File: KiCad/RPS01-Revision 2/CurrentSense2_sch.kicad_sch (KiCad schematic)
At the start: 6 parts

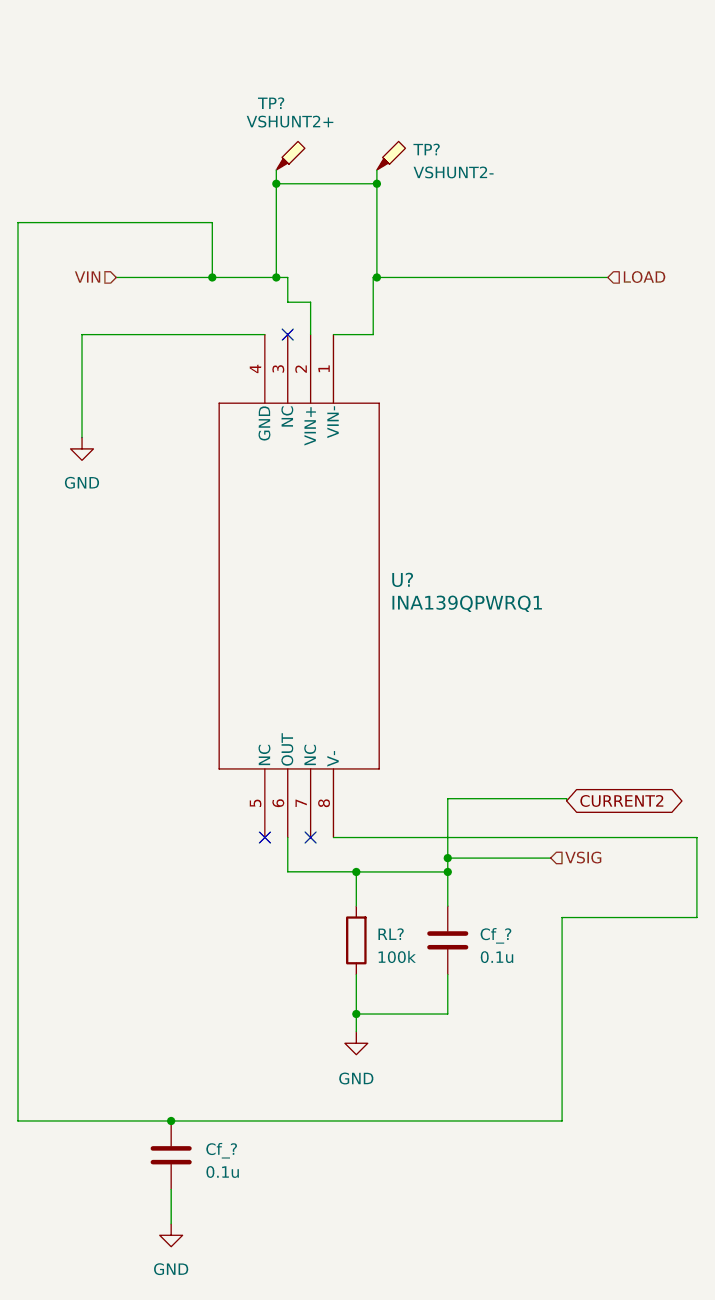
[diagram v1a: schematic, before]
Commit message: Current sense update
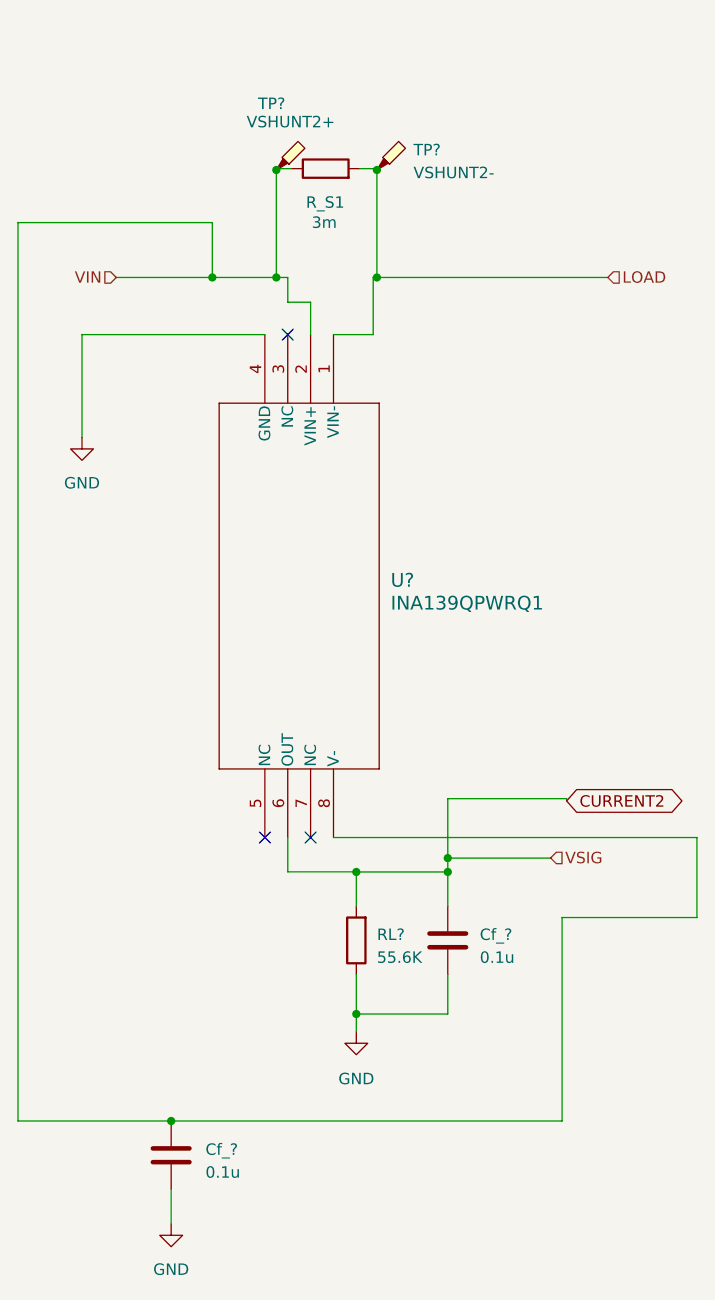
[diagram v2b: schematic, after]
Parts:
- added R_S1: 3m, Mechatronic Footprints:CSS2H-5930R, symbol Device:R
- RL?: value 100k -> 55.6K
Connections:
- net LOAD: now also R_S1.2; no longer Cf_?.1, TP?.1, U?.2 (VIN+), U?.8 (V-)
- new net VIN: Cf_?.1, R_S1.1, TP?.1, U?.2 (VIN+), U?.8 (V-)
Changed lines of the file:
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@@
 (kicad_sch (version 20230121) (generator eeschema)
   (paper "A4")
-  (junction (at 128.524 49.53) (diameter 0) (color 0 0 0 0)
+  (junction (at 128.524 48.006) (diameter 0) (color 0 0 0 0)
   )
   (junction (at 116.84 153.67) (diameter 0) (color 0 0 0 0)
@@
   (junction (at 147.574 124.46) (diameter 0) (color 0 0 0 0)
   )
-  (junction (at 139.7 49.53) (diameter 0) (color 0 0 0 0)
+  (junction (at 139.7 48.006) (diameter 0) (color 0 0 0 0)
   )
   (junction (at 137.414 141.7826) (diameter 0) (color 0 0 0 0)
@@
     (stroke (width 0) (type default))
   )
+  (wire (pts (xy 128.524 47.8536) (xy 128.524 48.006))
+    (stroke (width 0) (type default))
+  )
   (wire (pts (xy 129.794 125.984) (xy 137.414 125.984))
     (stroke (width 0) (type default))
@@
     (stroke (width 0) (type default))
   )
-  (wire (pts (xy 139.7 49.53) (xy 139.7 59.944))
-    (stroke (width 0) (type default))
-  )
-  (wire (pts (xy 128.524 49.53) (xy 139.7 49.53))
+  (wire (pts (xy 139.7 48.006) (xy 139.7 59.944))
     (stroke (width 0) (type default))
   )
@@
     (stroke (width 0) (type default))
   )
-  (wire (pts (xy 128.524 49.53) (xy 128.524 48.006))
+  (wire (pts (xy 130.2004 47.8536) (xy 128.524 47.8536))
     (stroke (width 0) (type default))
   )
@@
     (stroke (width 0) (type default))
   )
+  (wire (pts (xy 137.8204 47.8536) (xy 139.7 47.8536))
+    (stroke (width 0) (type default))
+  )
   (wire (pts (xy 134.874 122.174) (xy 175.26 122.174))
     (stroke (width 0) (type default))
@@
     (stroke (width 0) (type default))
   )
-  (wire (pts (xy 128.524 59.944) (xy 128.524 49.53))
+  (wire (pts (xy 128.524 48.006) (xy 128.524 59.944))
     (stroke (width 0) (type default))
   )
@@
     (stroke (width 0) (type default))
   )
+  (wire (pts (xy 139.7 47.8536) (xy 139.7 48.006))
+    (stroke (width 0) (type default))
+  )
   (wire (pts (xy 147.574 137.414) (xy 147.574 141.7826))
     (stroke (width 0) (type default))
@@
   )
   (wire (pts (xy 147.574 124.46) (xy 147.574 117.856))
-    (stroke (width 0) (type default))
-  )
-  (wire (pts (xy 139.7 48.006) (xy 139.7 49.53))
     (stroke (width 0) (type default))
   )
@@
       (effects (font (size 1.27 1.27)) (justify right))
     )
-    (property "Value" "100k" (at 139.7 135.509 0)
+    (property "Value" "55.6K" (at 139.7 135.509 0)
       (effects (font (size 1.27 1.27)) (justify right))
     )
@@
         )
       )
+    )
+  )
+  (symbol (lib_id "Device:R") (at 134.0104 47.8536 90) (unit 1)
+    (in_bom yes) (on_board yes) (dnp no)
+    (property "Reference" "R_S1" (at 133.9596 51.6128 90)
+      (effects (font (size 1.27 1.27)))
+    )
+    (property "Value" "3m" (at 133.858 53.848 90)
+      (effects (font (size 1.27 1.27)))
+    )
+    (property "Footprint" "Mechatronic Footprints:CSS2H-5930R" (at 134.0104 49.6316 90)
+      (effects (font (size 1.27 1.27)) hide)
+    )
+    (property "Datasheet" "~" (at 134.0104 47.8536 0)
+      (effects (font (size 1.27 1.27)) hide)
+    )
+    (pin "1")
+    (pin "2")
+    (instances
+      (project "rps01"
+        (path "/14930f15-c0a0-4b55-93e6-b112548415f6/13e150ee-6c46-47a5-9c09-3749eb0dcbfe"
+          (reference "R_S1") (unit 1)
+        )
+        (path "/14930f15-c0a0-4b55-93e6-b112548415f6/83d3dc76-6aeb-422d-8708-14a32de244f0"
+          (reference "R_S2") (unit 1)
+        )
+      )

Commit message: Update Current sense references
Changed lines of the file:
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@@
   )
   (symbol (lib_id "Device:R") (at 137.414 133.604 180) (unit 1)
-    (in_bom yes) (on_board yes) (dnp no) (fields_autoplaced)
-    (property "Reference" "RL?" (at 139.7 132.969 0)
+    (in_bom yes) (on_board yes) (dnp no)
+    (property "Reference" "RL?" (at 127 132.08 0)
       (effects (font (size 1.27 1.27)) (justify right))
     )
-    (property "Value" "55.6K" (at 139.7 135.509 0)
+    (property "Value" "55.6K" (at 127 134.62 0)
       (effects (font (size 1.27 1.27)) (justify right))
     )
@@
         )
         (path "/14930f15-c0a0-4b55-93e6-b112548415f6/83d3dc76-6aeb-422d-8708-14a32de244f0"
-          (reference "R31") (unit 1)
+          (reference "R1_CS2") (unit 1)
         )
       )
@@
         )
         (path "/14930f15-c0a0-4b55-93e6-b112548415f6/83d3dc76-6aeb-422d-8708-14a32de244f0"
-          (reference "C22") (unit 1)
+          (reference "C1_CS2") (unit 1)
         )
       )
@@
         )
         (path "/14930f15-c0a0-4b55-93e6-b112548415f6/83d3dc76-6aeb-422d-8708-14a32de244f0"
-          (reference "Cf_1") (unit 1)
-        )
-      )
+          (reference "C2_CS2") (unit 1)
+        )
+      )

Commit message: Only Switches left
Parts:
- removed Cf_?: 0.1u, Capacitor_SMD:C_0603_1608Metric, symbol Device:C
- added R_S1: 3m, Mechatronic Footprints:CSS2H-5930R, symbol Device:R
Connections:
- net LOAD: now also R_S1.2
- net VIN: now also R_S1.1

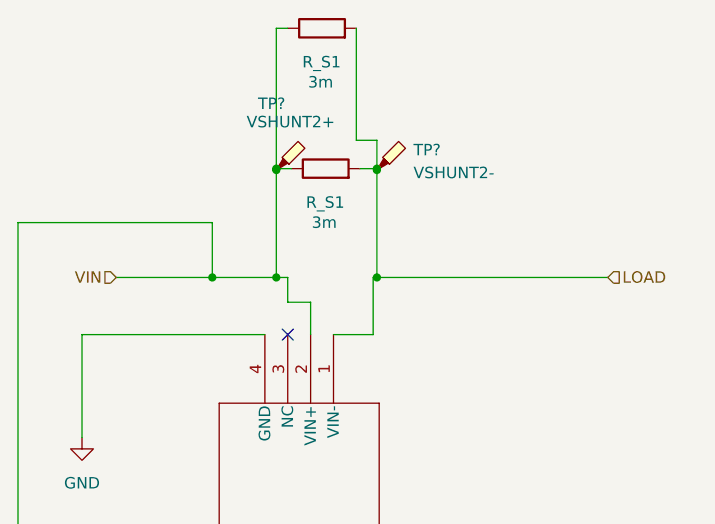
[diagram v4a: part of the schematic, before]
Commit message: Completed everything except the 3780 and the Polishing
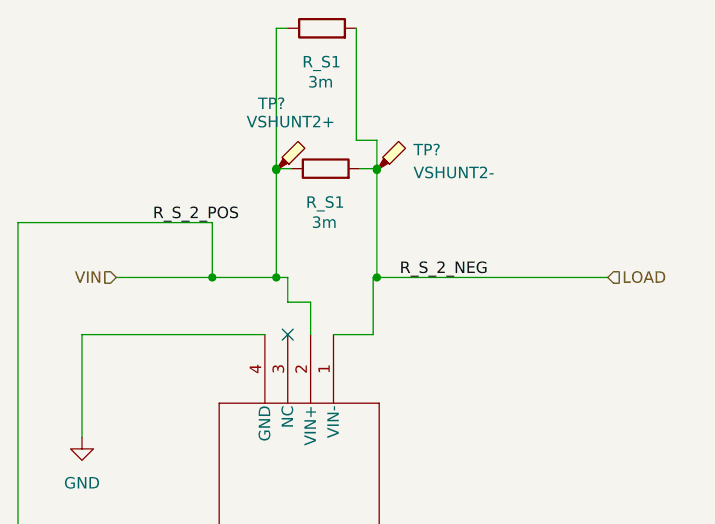
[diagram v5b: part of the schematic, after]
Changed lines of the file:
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@@
     (stroke (width 0) (type default))
+  )
+  (label "R_S_2_NEG" (at 142.24 59.944 0) (fields_autoplaced)
+    (effects (font (size 1.27 1.27)) (justify left bottom))
+  )
+  (label "R_S_2_POS" (at 114.808 53.848 0) (fields_autoplaced)
+    (effects (font (size 1.27 1.27)) (justify left bottom))
   )
   (global_label "CURRENT2" (shape bidirectional) (at 160.782 118.11 0) (fields_autoplaced)

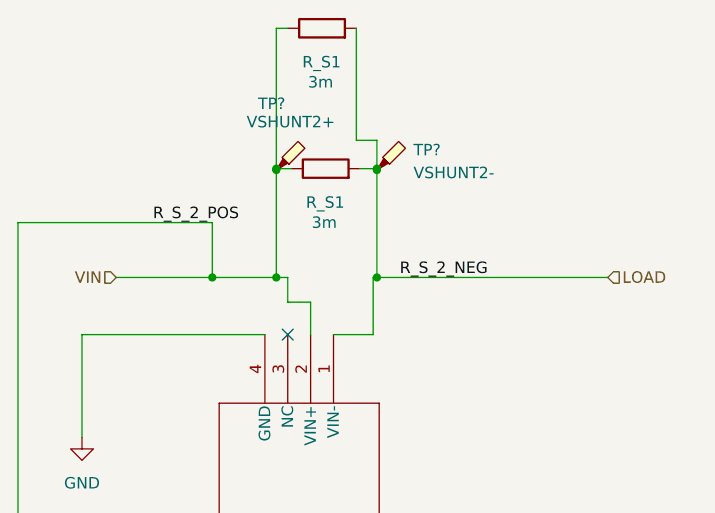
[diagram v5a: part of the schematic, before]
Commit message: Updated nets of Current 2 output and 3780 Globals.
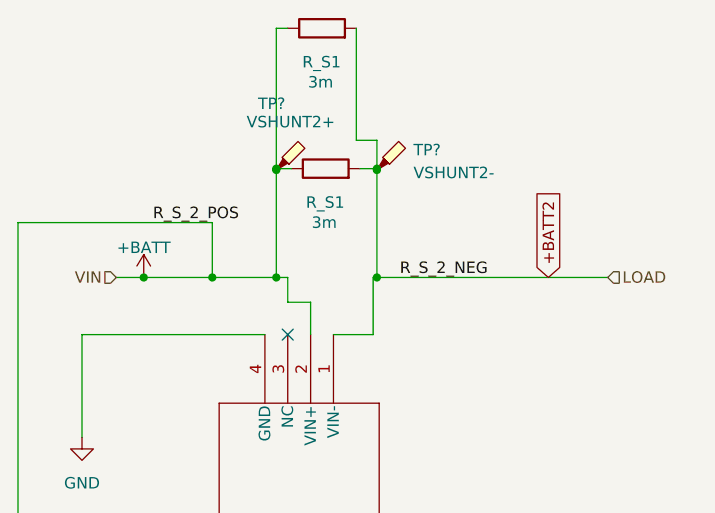
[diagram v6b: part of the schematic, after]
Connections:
- net LOAD renamed +BATT2
- net VIN renamed +BATT
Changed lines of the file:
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@@
   (junction (at 128.524 48.006) (diameter 0) (color 0 0 0 0)
+  )
+  (junction (at 113.792 59.944) (diameter 0) (color 0 0 0 0)
   )
   (junction (at 128.524 47.8536) (diameter 0) (color 0 0 0 0)
@@
     (stroke (width 0) (type default))
   )
+  (wire (pts (xy 113.792 59.944) (xy 121.412 59.944))
+    (stroke (width 0) (type default))
+  )
   (wire (pts (xy 147.574 124.46) (xy 159.004 124.46))
     (stroke (width 0) (type default))
@@
     (stroke (width 0) (type default))
   )
-  (wire (pts (xy 110.744 59.944) (xy 121.412 59.944))
+  (wire (pts (xy 110.744 59.944) (xy 113.792 59.944))
     (stroke (width 0) (type default))
   )
@@
     (effects (font (size 1.27 1.27)) (justify left bottom))
   )
+  (global_label "+BATT2" (shape input) (at 158.75 59.944 90) (fields_autoplaced)
+    (effects (font (size 1.27 1.27)) (justify left))
+    (property "Intersheetrefs" "${INTERSHEET_REFS}" (at 158.75 49.9625 90)
+      (effects (font (size 1.27 1.27)) (justify left) hide)
+    )
+  )
   (global_label "CURRENT2" (shape bidirectional) (at 160.782 118.11 0) (fields_autoplaced)
     (effects (font (size 1.27 1.27)) (justify left))
@@
     (effects (font (size 1.27 1.27)) (justify right))
   )
+  (symbol (lib_id "power:+BATT") (at 113.792 59.944 0) (unit 1)
+    (in_bom yes) (on_board yes) (dnp no) (fields_autoplaced)
+    (property "Reference" "#PWR03" (at 113.792 63.754 0)
+      (effects (font (size 1.27 1.27)) hide)
+    )
+    (property "Value" "+BATT" (at 113.792 56.642 0)
+      (effects (font (size 1.27 1.27)))
+    )
+    (property "Footprint" "" (at 113.792 59.944 0)
+      (effects (font (size 1.27 1.27)) hide)
+    )
+    (property "Datasheet" "" (at 113.792 59.944 0)
+      (effects (font (size 1.27 1.27)) hide)
+    )
+    (pin "1")
+    (instances
+      (project "rps01"
+        (path "/14930f15-c0a0-4b55-93e6-b112548415f6"
+          (reference "#PWR03") (unit 1)
+        )
+        (path "/14930f15-c0a0-4b55-93e6-b112548415f6/83d3dc76-6aeb-422d-8708-14a32de244f0"
+          (reference "#PWR035") (unit 1)
+        )
+      )
+    )
+  )
   (symbol (lib_id "power:GND") (at 137.414 143.764 0) (unit 1)
